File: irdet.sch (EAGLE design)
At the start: 66 parts, among them IC1 MEGA8-AI, IC2 78L05F, J1 PSH02-04WG, J2 PSH02-04WG, J3 PSH02-04WG, J4 PSH02-04WG, J5 22-05-7098-09, T1 S9013, T2 S9012, T3 S9013, T4 S9012, T5 S9013, T6 S9012, T7 S9013, T8 S9012, X1 ARK500/2

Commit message: Fix wire name.
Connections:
- removed net MOSI: ISP1.MOSI
- net MOSI/IN7: now also ISP1.MOSI
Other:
- moved on the sheet: C3
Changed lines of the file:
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@@
 <attribute name="VALUE" x="210.82" y="134.62" size="1.778" layer="96"/>
 </instance>
-<instance part="C3" gate="G$1" x="223.52" y="147.32" smashed="yes">
-<attribute name="NAME" x="225.044" y="147.701" size="1.778" layer="95"/>
-<attribute name="VALUE" x="225.044" y="142.621" size="1.778" layer="96"/>
+<instance part="C3" gate="G$1" x="228.6" y="147.32" smashed="yes">
+<attribute name="NAME" x="230.124" y="147.701" size="1.778" layer="95"/>
+<attribute name="VALUE" x="230.124" y="142.621" size="1.778" layer="96"/>
 </instance>
 <instance part="X1" gate="-1" x="27.94" y="231.14" smashed="yes" rot="MR0">
@@
 <pinref part="C3" gate="G$1" pin="2"/>
 <wire x1="213.36" y1="142.24" x2="213.36" y2="139.7" width="0.1524" layer="91"/>
-<wire x1="223.52" y1="142.24" x2="213.36" y2="142.24" width="0.1524" layer="91"/>
+<wire x1="228.6" y1="142.24" x2="213.36" y2="142.24" width="0.1524" layer="91"/>
 <junction x="213.36" y="142.24"/>
 </segment>
@@
 </segment>
 </net>
-<net name="MOSI" class="0">
-<segment>
-<pinref part="ISP1" gate="G$1" pin="MOSI"/>
-<wire x1="210.82" y1="147.32" x2="213.36" y2="147.32" width="0.1524" layer="91"/>
-<label x="213.36" y="147.32" size="1.27" layer="95" xref="yes"/>
-</segment>
-</net>
 <net name="+5V" class="3">
 <segment>
@@
 <wire x1="213.36" y1="149.86" x2="213.36" y2="152.4" width="0.1524" layer="91"/>
 <pinref part="C3" gate="G$1" pin="1"/>
-<wire x1="213.36" y1="149.86" x2="223.52" y2="149.86" width="0.1524" layer="91"/>
+<wire x1="213.36" y1="149.86" x2="228.6" y2="149.86" width="0.1524" layer="91"/>
 <junction x="213.36" y="149.86"/>
 </segment>
@@
 <label x="86.36" y="30.48" size="1.27" layer="95" xref="yes"/>
 </segment>
-</net>
+<segment>
+<pinref part="ISP1" gate="G$1" pin="MOSI"/>
+<wire x1="210.82" y1="147.32" x2="213.36" y2="147.32" width="0.1524" layer="91"/>
+<label x="213.36" y="147.32" size="1.27" layer="95" xref="yes"/>
+</segment>
+</net>

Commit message: Add board.
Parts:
- R10, R4, R5, R6, R8, R9: value (none) -> 1k
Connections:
- net N$1: now also RN1.1; no longer RN1.4
- net N$2: now also RN1.2; no longer RN1.3
- net N$26: now also OK1D.COL; no longer OK1A.COL
- net N$27: now also OK1C.COL; no longer OK1B.COL
- net N$28: now also OK1B.COL; no longer OK1C.COL
- net N$29: now also OK1A.COL; no longer OK1D.COL
- net N$3: now also RN3.1; no longer RN3.4
- net N$30: now also J5-7.S, OK2B.COL; no longer J5-5.S, OK2A.COL
- net N$31: now also J5-8.S, OK2A.COL; no longer J5-6.S, OK2B.COL
- net N$32: now also J5-6.S; no longer J5-7.S
- net N$33: now also J5-5.S; no longer J5-8.S
- net N$4: now also RN3.2; no longer RN3.3
- net N$5: now also RN1.3; no longer RN1.2
- net N$6: now also RN1.4; no longer RN1.1
- net N$7: now also RN3.3; no longer RN3.2
- net N$8: now also RN3.4; no longer RN3.1
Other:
- moved on the sheet: J5-1, J5-2, J5-3, J5-4, J5-5, J5-6, J5-7, J5-8, R10, R4, R5, R6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

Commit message: Add rest of PCB.
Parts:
- removed C3: 100n, rcl:C-EUC0805
- added X2: ARK500/2, con-malina:ARK500/2
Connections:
- removed net MISO: IC1.PB4(MISO), ISP1.MISO
- removed net MOSI/IN7: C14.1, IC1.PB3(MOSI/OC2), ISP1.MOSI, RN4.2
- removed net N$34: F1.1, X1-1.1
- removed net OUT1: IC1.PD0(RXD), R3.1
- removed net OUT2: IC1.PD1(TXD), R4.1
- new net +12VIN: F1.1, X1-2.1, X2-1.1
- new net IN7: C14.1, IC1.PD2(INT0), RN4.2
- new net MISO/OUT1: IC1.PB4(MISO), ISP1.MISO, R7.1
- new net MOSI/OUT2: IC1.PB3(MOSI/OC2), ISP1.MOSI, R8.1
- net +5V: no longer C3.1
- net CPUPOW1-2: now also IC1.PC0(ADC0); no longer IC1.PB0(ICP)
- net CPUPOW3-4: now also IC1.PC1(ADC1); no longer IC1.PB1(OC1A)
- net CPUPOW5-6: now also IC1.PD4(XCK/T0); no longer IC1.PB2(SS/OC1B)
- net GND: now also X1-1.1, X2-2.1; no longer C3.2, X1-2.1
- net IN1: now also IC1.PC2(ADC2); no longer IC1.PC0(ADC0)
- net IN2: now also IC1.PC3(ADC3); no longer IC1.PC1(ADC1)
- net IN3: now also IC1.PC5(ADC5/SCL); no longer IC1.PC2(ADC2)
- net IN4: now also IC1.PC4(ADC4/SDA); no longer IC1.PC3(ADC3)
- net IN5: now also IC1.PD1(TXD); no longer IC1.PC4(ADC4/SDA)
- net IN6: now also IC1.PD0(RXD); no longer IC1.PC5(ADC5/SCL)
- net IN8: now also IC1.PD3(INT1); no longer IC1.PB7(XTAL2/TOSC2)
- net OUT3: now also IC1.PB2(SS/OC1B), R9.1; no longer IC1.PD2(INT0), R5.1
- net OUT4: now also IC1.PB1(OC1A), R10.1; no longer IC1.PD3(INT1), R6.1
- net OUT5: now also IC1.PB0(ICP), R3.1; no longer IC1.PD4(XCK/T0), R7.1
- net OUT6: now also IC1.PD7(AIN1), R4.1; no longer IC1.PD5(T1), R8.1
- net OUT7: now also R5.1; no longer R9.1
- net OUT8: now also IC1.PD5(T1), R6.1; no longer IC1.PD7(AIN1), R10.1
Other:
- moved on the sheet: X1-1, X1-2

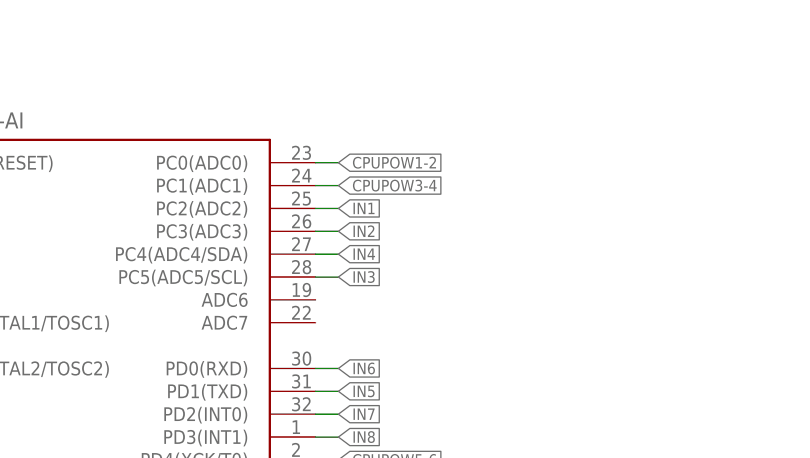
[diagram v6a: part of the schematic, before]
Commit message: Brd: add texts, position names on silkscreen.
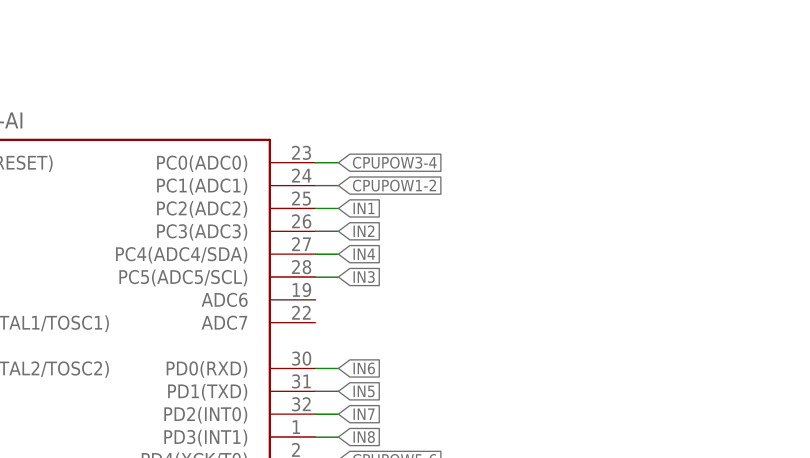
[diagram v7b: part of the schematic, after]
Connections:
- net CPUPOW1-2: now also IC1.PC1(ADC1); no longer IC1.PC0(ADC0)
- net CPUPOW3-4: now also IC1.PC0(ADC0); no longer IC1.PC1(ADC1)
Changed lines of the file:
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@@
 </segment>
 <segment>
-<pinref part="IC1" gate="G$1" pin="PC1(ADC1)"/>
-<wire x1="220.98" y1="231.14" x2="223.52" y2="231.14" width="0.1524" layer="91"/>
-<label x="223.52" y="231.14" size="1.27" layer="95" xref="yes"/>
+<pinref part="IC1" gate="G$1" pin="PC0(ADC0)"/>
+<wire x1="220.98" y1="233.68" x2="223.52" y2="233.68" width="0.1524" layer="91"/>
+<label x="223.52" y="233.68" size="1.27" layer="95" xref="yes"/>
 </segment>
 </net>
@@
 </segment>
 <segment>
-<pinref part="IC1" gate="G$1" pin="PC0(ADC0)"/>
-<wire x1="220.98" y1="233.68" x2="223.52" y2="233.68" width="0.1524" layer="91"/>
-<label x="223.52" y="233.68" size="1.27" layer="95" xref="yes"/>
+<pinref part="IC1" gate="G$1" pin="PC1(ADC1)"/>
+<wire x1="220.98" y1="231.14" x2="223.52" y2="231.14" width="0.1524" layer="91"/>
+<label x="223.52" y="231.14" size="1.27" layer="95" xref="yes"/>
 </segment>
 </net>

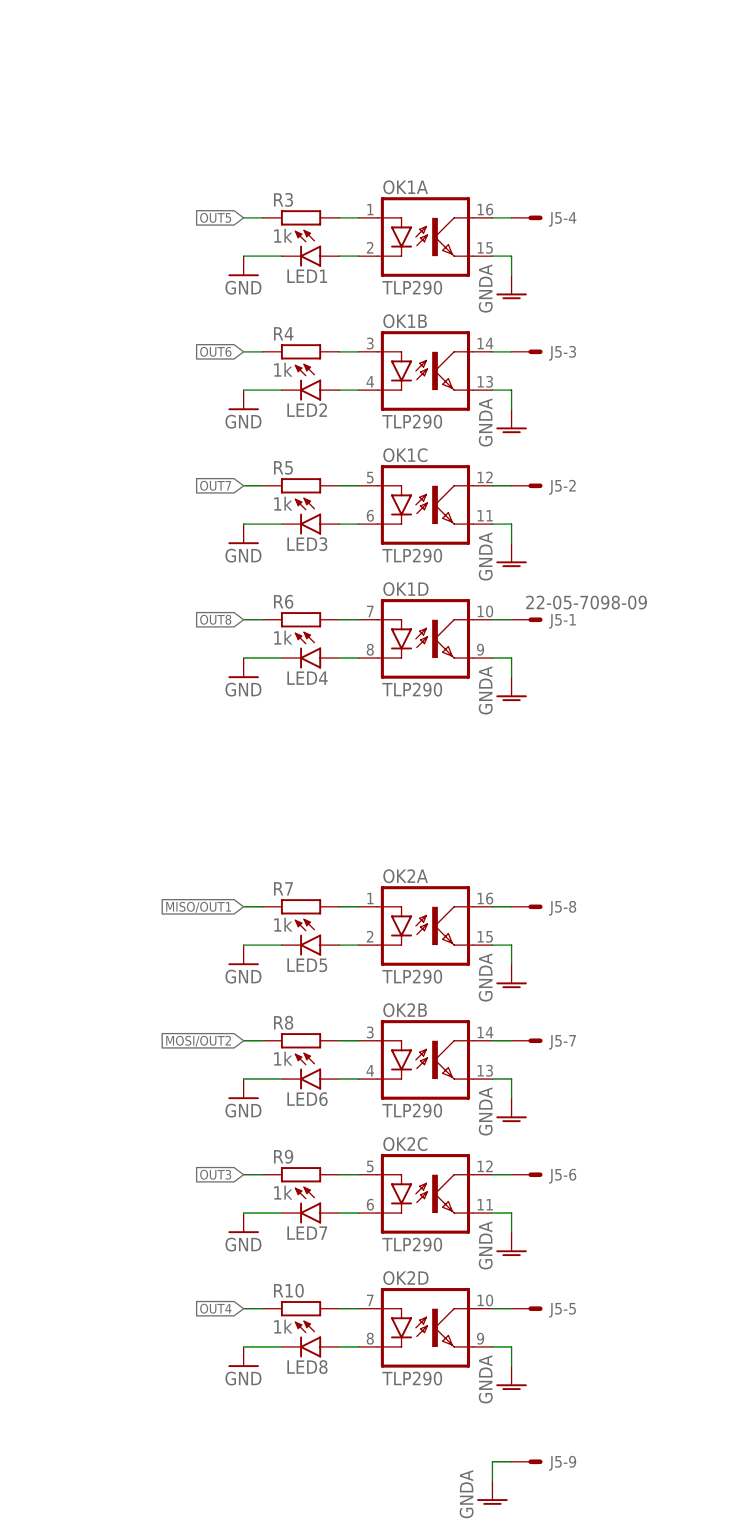
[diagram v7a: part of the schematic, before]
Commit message: Fix parts names.
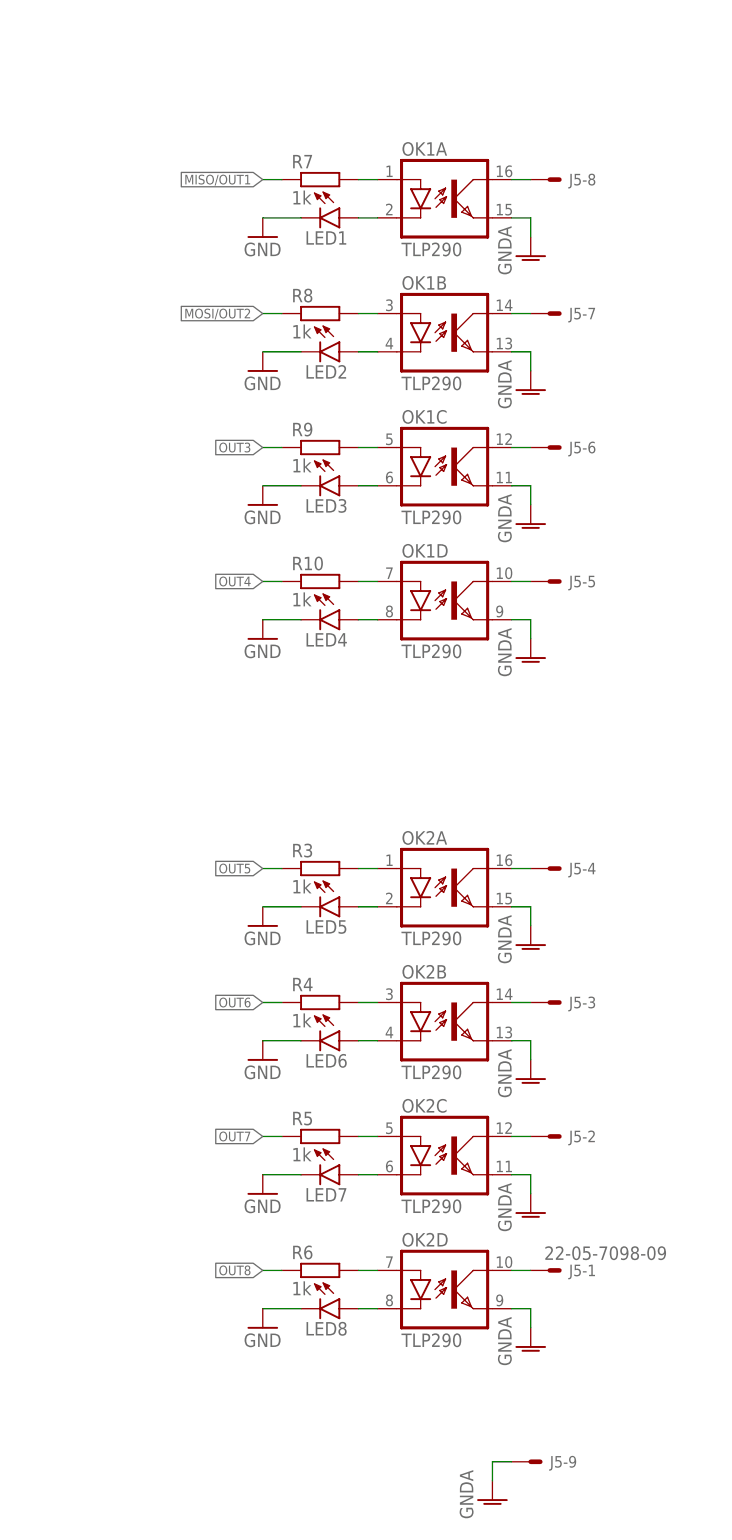
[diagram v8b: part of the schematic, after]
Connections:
- net N$10: now also OK2A.A; no longer OK1A.A
- net N$11: now also OK2D.A; no longer OK1D.A
- net N$12: now also OK2C.A; no longer OK1C.A
- net N$14: now also OK2B.A; no longer OK1B.A
- net N$19: now also OK1A.A; no longer OK2A.A
- net N$20: now also OK1D.A; no longer OK2D.A
- net N$21: now also OK1C.A; no longer OK2C.A
- net N$22: now also OK1B.A; no longer OK2B.A
- net N$26: now also OK2D.COL; no longer OK1D.COL
- net N$27: now also OK2C.COL; no longer OK1C.COL
- net N$28: now also OK2B.COL; no longer OK1B.COL
- net N$29: now also OK2A.COL; no longer OK1A.COL
- net N$30: now also OK1B.COL; no longer OK2B.COL
- net N$31: now also OK1A.COL; no longer OK2A.COL
- net N$32: now also OK1C.COL; no longer OK2C.COL
- net N$33: now also OK1D.COL; no longer OK2D.COL
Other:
- moved on the sheet: J5-1, J5-2, J5-3, J5-4, J5-5, J5-6, J5-7, J5-8, LED1, LED2, LED3, LED4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
